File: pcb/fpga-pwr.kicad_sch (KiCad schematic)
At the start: 6 parts, among them M1V0 TestPoint, M1V2 TestPoint, U5 XC7A35T-FGG484

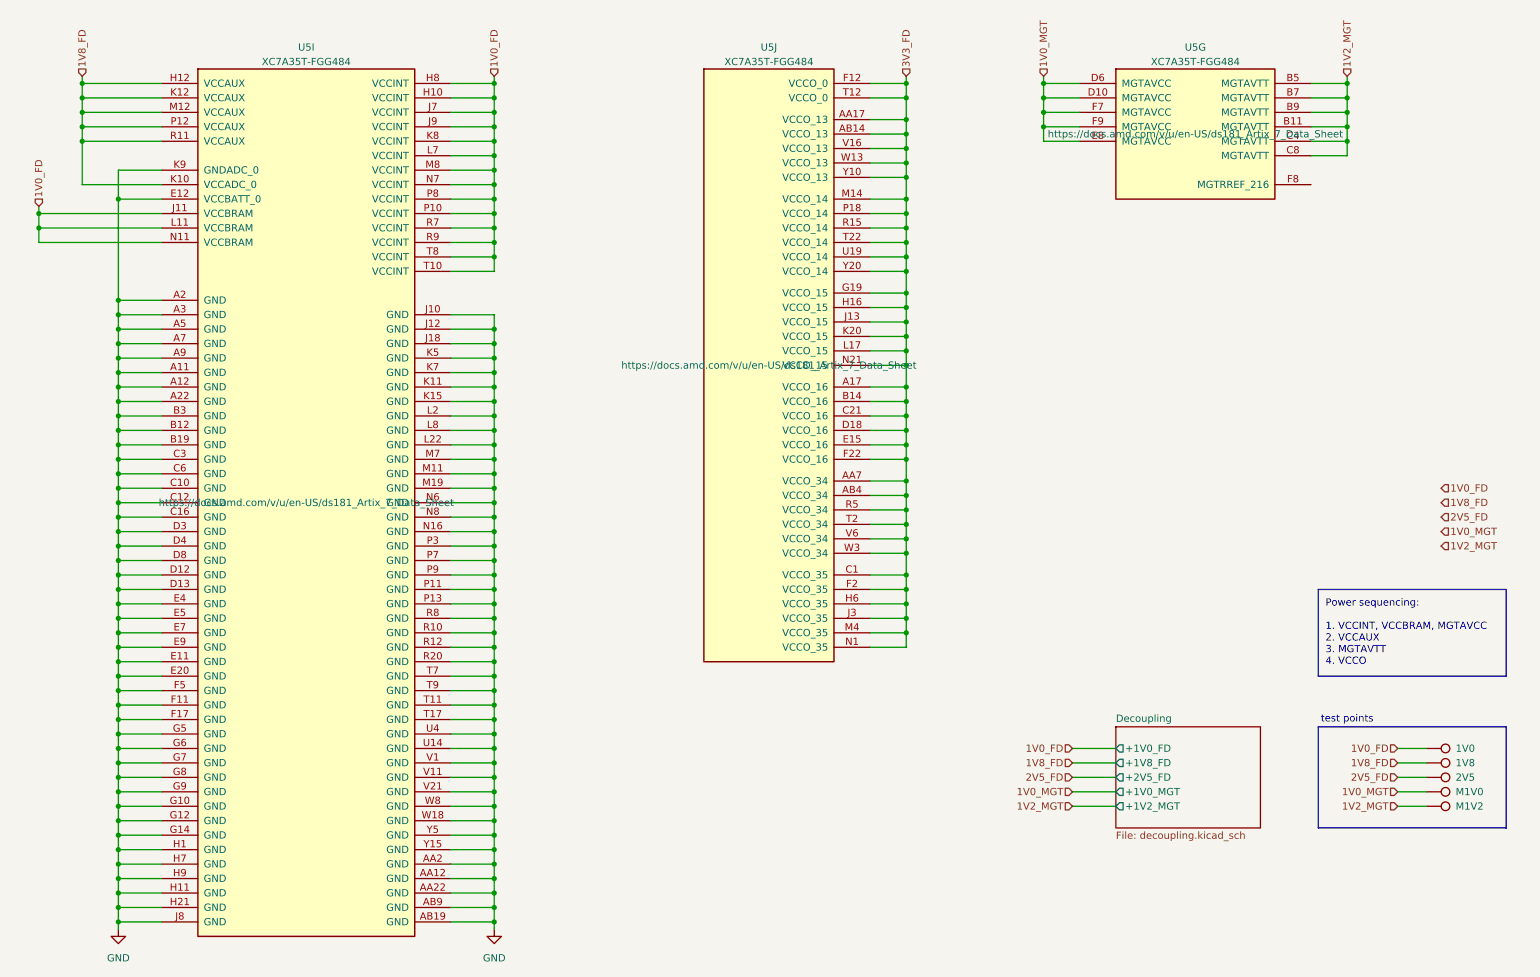
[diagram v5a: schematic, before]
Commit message: power flags
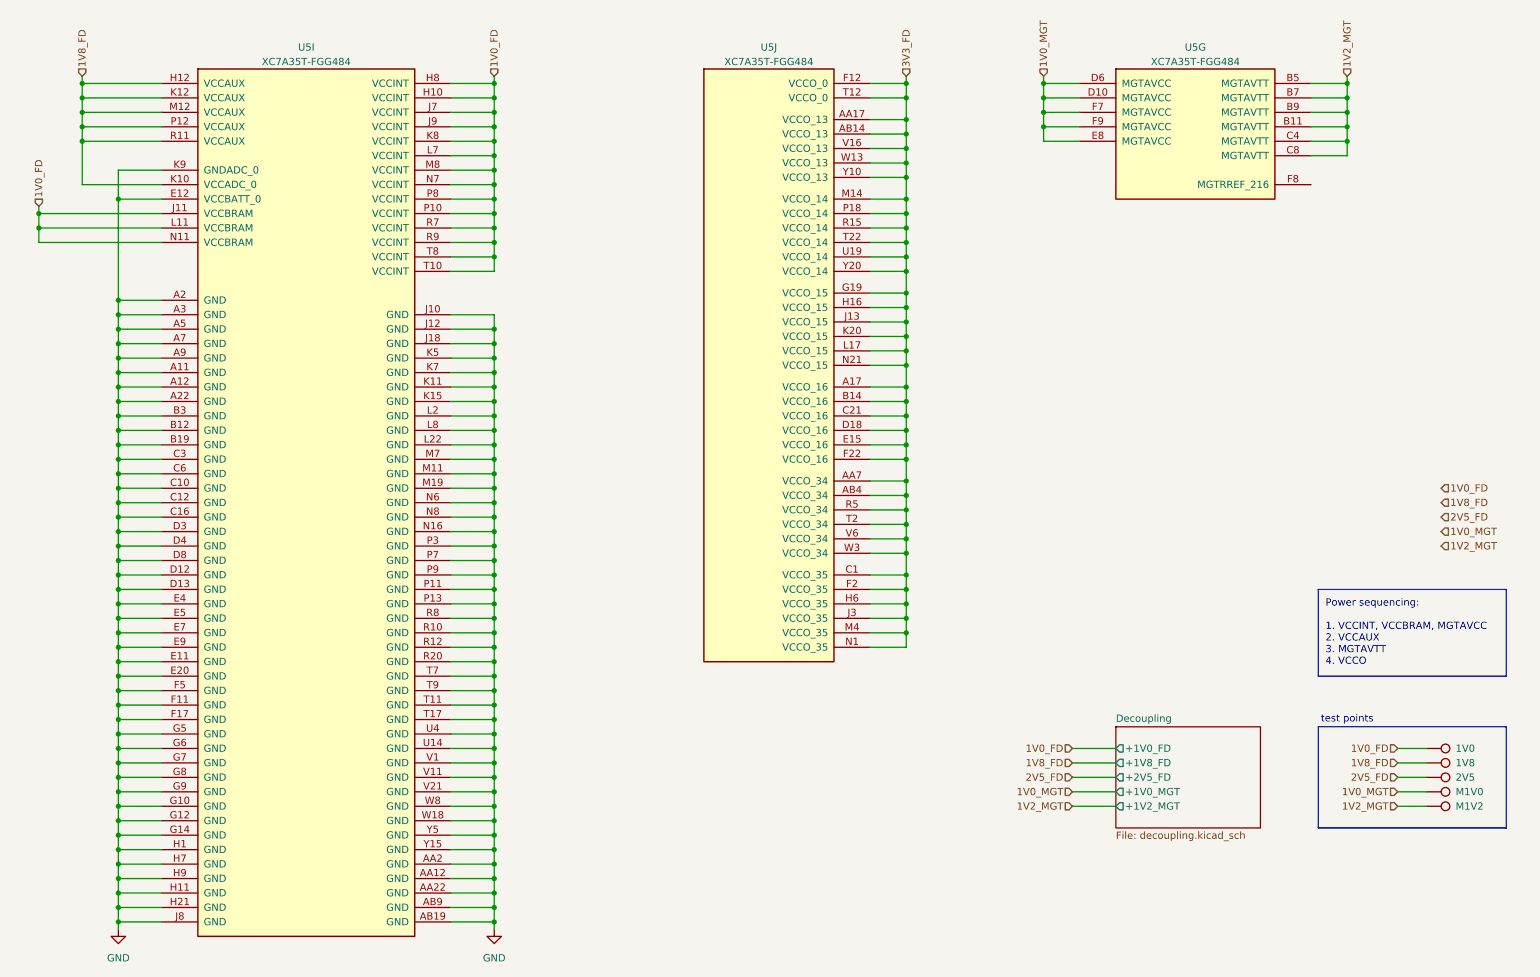
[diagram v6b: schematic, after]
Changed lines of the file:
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@@
 					(size 1.27 1.27)
 				)
+				(hide yes)
 			)
 		)
@@
 					(size 1.27 1.27)
 				)
+				(hide yes)
 			)
 		)
@@
 					(size 1.27 1.27)
 				)
-			)
-		)
+				(hide yes)
+			)
+		)

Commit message: fpga decoupling
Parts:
- renumbered 2V5 to 3V3
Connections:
- net 2V5_FD is gone; now on net 3V3_FD: 3V3.1
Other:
- sheet Decoupling ports: added 1V0_FD, 1V0_MGT, 1V2_MGT, 1V8_FD, 3V3_FD; removed +1V0_FD, +1V0_MGT, +1V2_MGT, +1V8_FD, +2V5_FD
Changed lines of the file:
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@@
 		)
 	)
-	(hierarchical_label "1V8_FD"
-		(shape input)
-		(at 266.7 102.87 0)
-		(effects
-			(font
-				(size 1.27 1.27)
-			)
-			(justify left)
-		)
-	)
 	(hierarchical_label "1V2_MGT"
 		(shape input)
@@
 	(hierarchical_label "1V0_MGT"
 		(shape input)
-		(at 266.7 107.95 0)
-		(effects
-			(font
-				(size 1.27 1.27)
-			)
-			(justify left)
-		)
-	)
-	(hierarchical_label "1V0_MGT"
-		(shape input)
 		(at 201.93 153.67 180)
 		(effects
@@
 	(hierarchical_label "1V0_FD"
 		(shape input)
-		(at 266.7 100.33 0)
-		(effects
-			(font
-				(size 1.27 1.27)
-			)
-			(justify left)
-		)
-	)
-	(hierarchical_label "2V5_FD"
-		(shape input)
-		(at 266.7 105.41 0)
-		(effects
-			(font
-				(size 1.27 1.27)
-			)
-			(justify left)
-		)
-	)
-	(hierarchical_label "1V0_FD"
-		(shape input)
 		(at 20.32 50.8 90)
 		(effects
@@
 		)
 	)
-	(hierarchical_label "2V5_FD"
+	(hierarchical_label "3V3_FD"
 		(shape input)
 		(at 201.93 151.13 180)
@@
 		)
 	)
-	(hierarchical_label "1V2_MGT"
-		(shape input)
-		(at 266.7 110.49 0)
-		(effects
-			(font
-				(size 1.27 1.27)
-			)
-			(justify left)
-		)
-	)
 	(hierarchical_label "1V0_FD"
 		(shape input)
@@
 		)
 	)
-	(hierarchical_label "2V5_FD"
+	(hierarchical_label "3V3_FD"
 		(shape input)
 		(at 259.08 151.13 180)
@@
 		(on_board yes)
 		(dnp no)
-		(property "Reference" "2V5"
+		(property "Reference" "3V3"
 			(at 269.24 151.13 90)
 			(effects
@@
 			(project "RPi-HwAB-1"
 				(path "/e63e39d7-6ac0-4ffd-8aa3-1841a4541b55/59d21473-a004-4514-8090-fd93db818925/94db1840-7840-4b32-9939-76c2575d480c"
-					(reference "2V5")
+					(reference "3V3")
 					(unit 1)
 				)
@@
 			)
 		)
-		(pin "+1V0_FD" output
+		(pin "1V0_FD" input
 			(at 209.55 146.05 180)
 			(effects
@@
 			)
 		)
-		(pin "+1V0_MGT" output
+		(pin "1V0_MGT" input
 			(at 209.55 153.67 180)
 			(effects
@@
 			)
 		)
-		(pin "+1V2_MGT" output
+		(pin "1V2_MGT" input
 			(at 209.55 156.21 180)
 			(effects
@@
 			)
 		)
-		(pin "+1V8_FD" output
+		(pin "1V8_FD" input
 			(at 209.55 148.59 180)
 			(effects
@@
 			)
 		)
-		(pin "+2V5_FD" output
+		(pin "3V3_FD" input
 			(at 209.55 151.13 180)
 			(effects

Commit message: saved libraries to project
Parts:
- 1V0, 1V8, 3V3, M1V0, M1V2: symbol Connector:TestPoint -> library:TestPoint
- U5: symbol FPGA_Xilinx_Artix7:XC7A35T-FGG484 -> library:XC7A35T-FGG484
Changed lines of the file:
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@@
 	)
 	(symbol
-		(lib_id "Connector:TestPoint")
+		(lib_id "library:TestPoint")
 		(at 264.16 146.05 270)
 		(unit 1)
@@
 	)
 	(symbol
-		(lib_id "power:GND")
+		(lib_id "library:GND")
 		(at 100.33 177.8 0)
 		(unit 1)
@@
 	)
 	(symbol
-		(lib_id "Connector:TestPoint")
+		(lib_id "library:TestPoint")
 		(at 264.16 151.13 270)
 		(unit 1)
@@
 	)
 	(symbol
-		(lib_id "Connector:TestPoint")
+		(lib_id "library:TestPoint")
 		(at 264.16 156.21 270)
 		(unit 1)
@@
 	)
 	(symbol
-		(lib_id "FPGA_Xilinx_Artix7:XC7A35T-FGG484")
+		(lib_id "library:XC7A35T-FGG484")
 		(at 223.52 38.1 0)
 		(unit 7)
@@
 	)
 	(symbol
-		(lib_id "Connector:TestPoint")
+		(lib_id "library:TestPoint")
 		(at 264.16 153.67 270)
 		(unit 1)
@@
 	)
 	(symbol
-		(lib_id "FPGA_Xilinx_Artix7:XC7A35T-FGG484")
+		(lib_id "library:XC7A35T-FGG484")
 		(at 148.59 78.74 0)
 		(unit 10)
@@
 	)
 	(symbol
-		(lib_id "power:GND")
+		(lib_id "library:GND")
 		(at 34.29 177.8 0)
 		(unit 1)
@@
 	)
 	(symbol
-		(lib_id "FPGA_Xilinx_Artix7:XC7A35T-FGG484")
+		(lib_id "library:XC7A35T-FGG484")
 		(at 67.31 102.87 0)
 		(unit 9)
@@
 	)
 	(symbol
-		(lib_id "Connector:TestPoint")
+		(lib_id "library:TestPoint")
 		(at 264.16 148.59 270)
 		(unit 1)
